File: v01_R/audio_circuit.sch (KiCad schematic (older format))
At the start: 44 parts, among them P1 CONN_1, P10 CONN_1, P11 CONN_1, P12 CONN_1, P2 CONN_1, P3 CONN_1, P4 CONN_1, P5 CONN_1, P6 CONN_1, P7 CONN_1, P8 CONN_1, P9 CONN_1, U2 TI_TPA6138A2

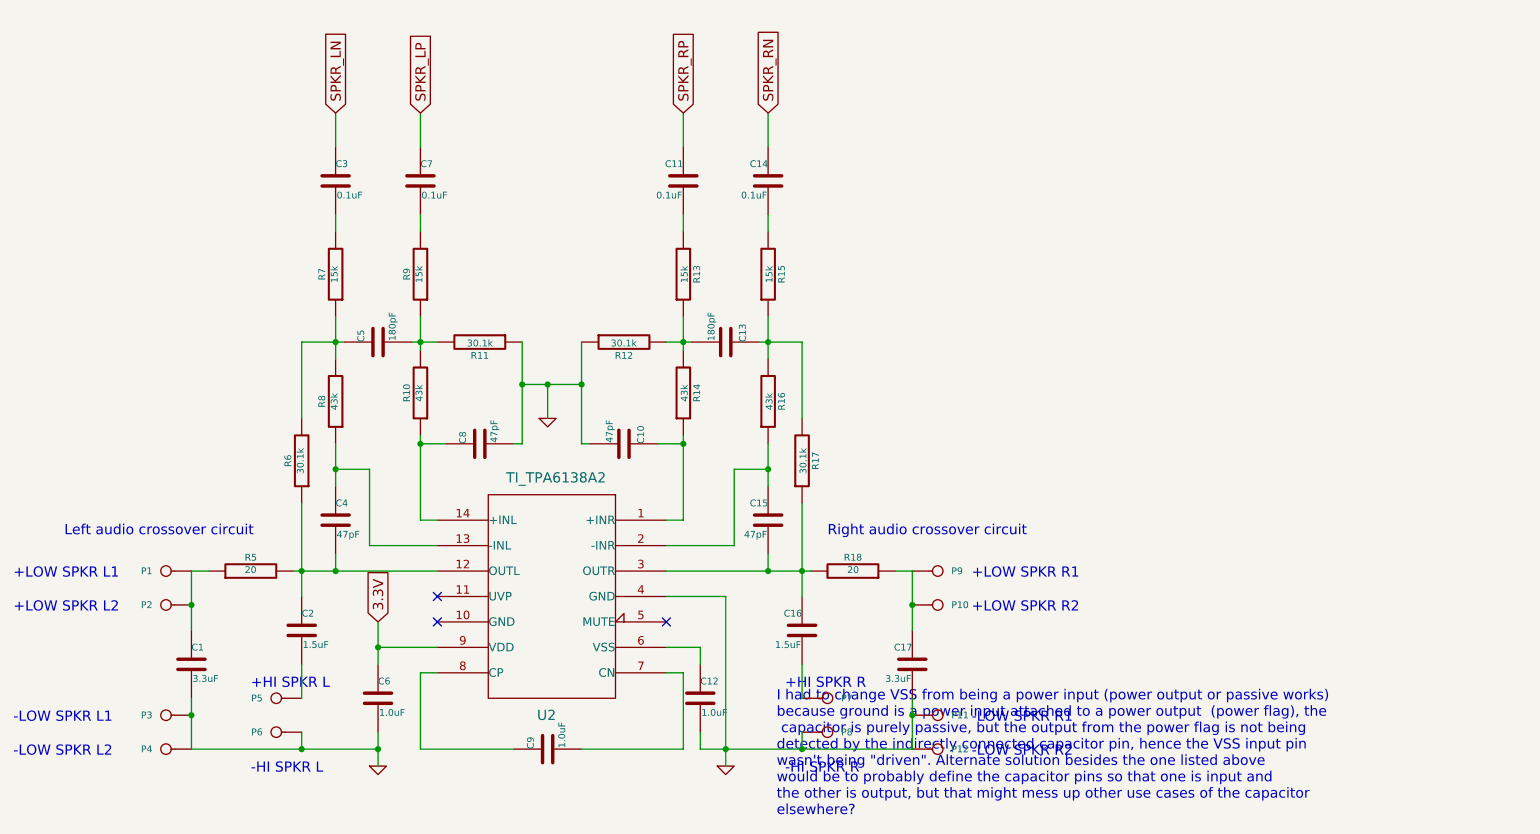
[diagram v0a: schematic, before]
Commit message: Update removes the left channel of the audio circuit.
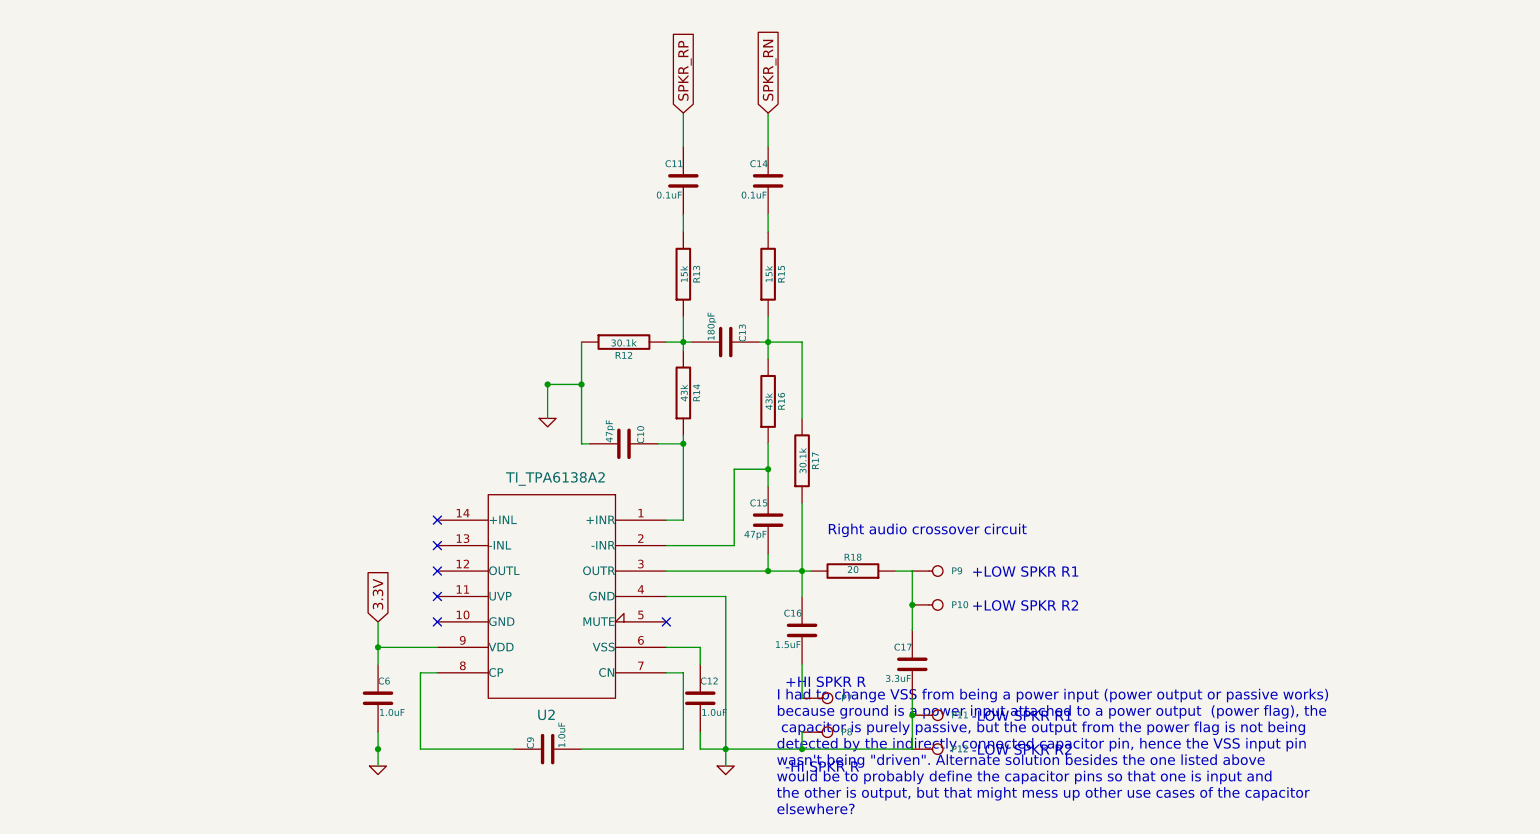
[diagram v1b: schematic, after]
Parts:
- removed C1: 3.3uF, ~, symbol C
- removed C2: 1.5uF, ~, symbol C
- removed C3, C7: 0.1uF, ~, symbol C
- removed C4, C8: 47pF, ~, symbol C
- removed C5: 180pF, ~, symbol C
- removed P1, P2, P3, P4, P5, P6: CONN_1, symbol CONN_1
- removed R10, R8: 43k, ~, symbol R
- removed R11, R6: 30.1k, ~, symbol R
- removed R5: 20, ~, symbol R
- removed R7, R9: 15k, ~, symbol R
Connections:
- no-connect marks 3 -> 6
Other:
- note removed: "+HI SPKR L"
- note removed: "+LOW SPKR L1"
- note removed: "+LOW SPKR L2"
- note removed: "-HI SPKR L"
- note removed: "-LOW SPKR L1"
- note removed: "-LOW SPKR L2"
- note removed: "Left audio crossover circuit"

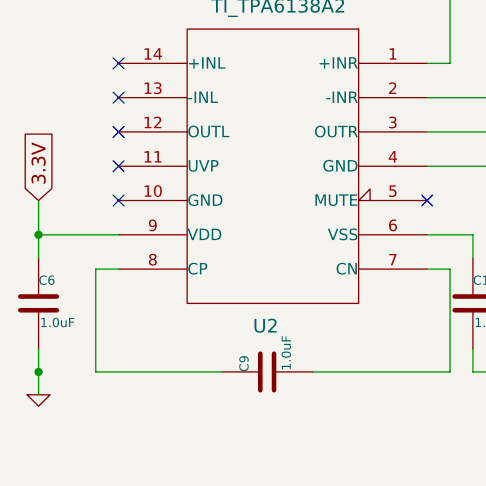
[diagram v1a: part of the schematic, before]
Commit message: Updating entire schematic and footprint selections. Adding jst-ph footprints.
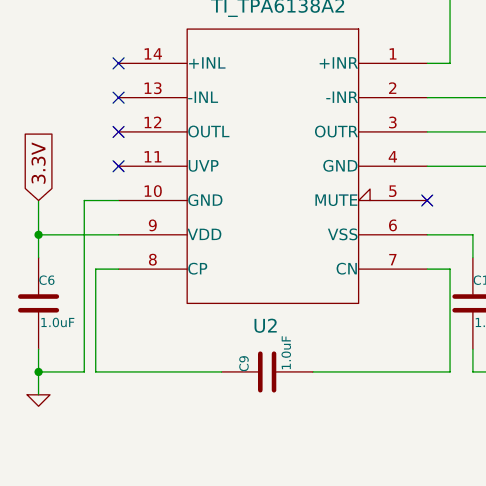
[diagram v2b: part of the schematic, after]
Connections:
- net GND: now also U2.10 (GND)
- no-connect marks 6 -> 5
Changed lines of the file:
@@
 Sheet 2 4
 Title ""
-Date "16 jan 2015"
+Date "17 jan 2015"
 Rev ""
 Comp ""
@@
 $EndComp
 $Comp
-L GND #PWR05
+L GND #PWR04
 U 1 1 541DFF4B
 P 4800 6150
-F 0 "#PWR05" H 4800 6150 30  0001 C CNN
+F 0 "#PWR04" H 4800 6150 30  0001 C CNN
 F 1 "GND" H 4800 6080 30  0001 C CNN
 F 2 "" H 4800 6150 60  0000 C CNN
@@
 $EndComp
 NoConn ~ 5150 5150
-NoConn ~ 5150 5300
-$Comp
-L GND #PWR06
+$Comp
+L GND #PWR05
 U 1 1 541E060D
 P 5800 4100
-F 0 "#PWR06" H 5800 4100 30  0001 C CNN
+F 0 "#PWR05" H 5800 4100 30  0001 C CNN
 F 1 "GND" H 5800 4030 30  0001 C CNN
 F 2 "" H 5800 4100 60  0000 C CNN
@@
 $EndComp
 $Comp
-L GND #PWR07
+L GND #PWR06
 U 1 1 541E08B0
 P 6850 6150
-F 0 "#PWR07" H 6850 6150 30  0001 C CNN
+F 0 "#PWR06" H 6850 6150 30  0001 C CNN
 F 1 "GND" H 6850 6080 30  0001 C CNN
 F 2 "" H 6850 6150 60  0000 C CNN
@@
 	1    0    0    -1
 $EndComp
-NoConn ~ 6500 5300
 Text Notes 7450 4800 0    60   ~ 0
 Right audio crossover circuit
@@
 NoConn ~ 5150 4850
 NoConn ~ 5150 5000
+Wire Wire Line
+	5150 5300 5000 5300
+Wire Wire Line
+	5000 5300 5000 6050
+Wire Wire Line
+	5000 6050 4800 6050
+NoConn ~ 6500 5300
 $EndSCHEMATC

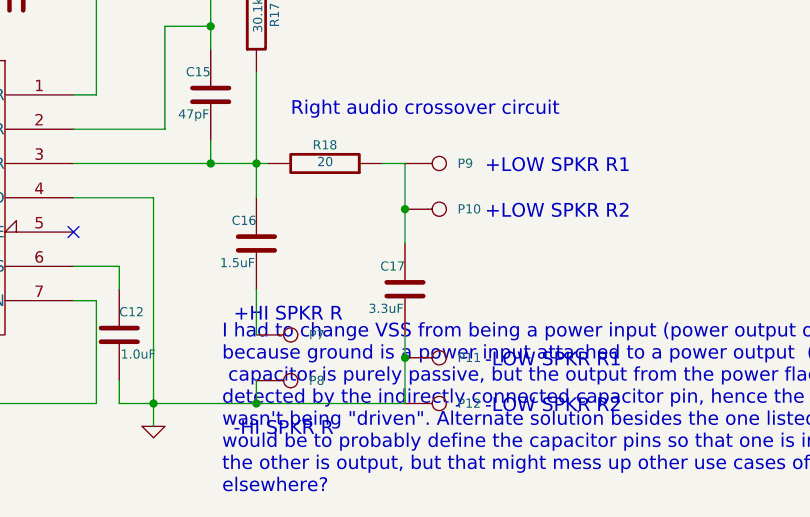
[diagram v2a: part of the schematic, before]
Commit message: Adding very rough initial version of PCB. The BA driver pads were not exact yet (based off of a Sonion driver datasheet).
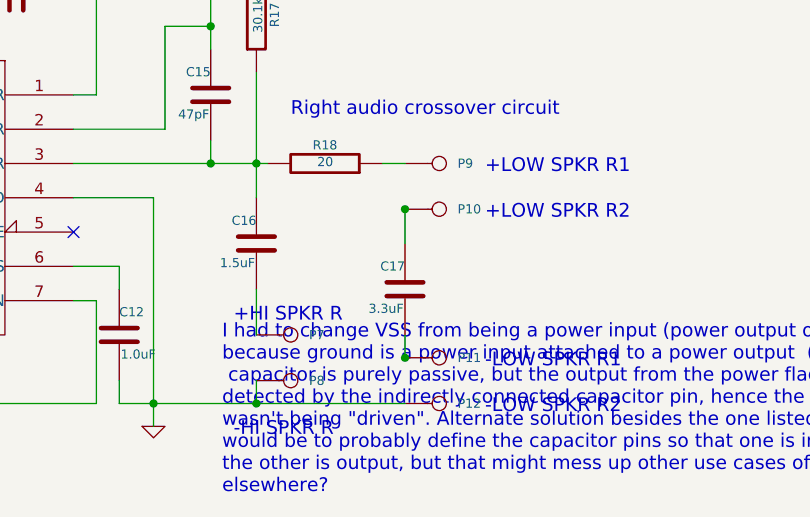
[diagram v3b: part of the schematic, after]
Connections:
- net GND: no longer C17.2, P11.1
- net at C17.1, P10.1: no longer P9.1, R18.1
- new net: C17.2, P11.1
- new net: P9.1, R18.1
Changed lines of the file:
@@
 Sheet 2 4
 Title ""
-Date "17 jan 2015"
+Date "18 jan 2015"
 Rev ""
 Comp ""
@@
 	7300 6050 7300 5950
 Connection ~ 7300 6050
-Wire Wire Line
-	7950 5750 7950 6050
 Connection ~ 7950 5850
-Wire Wire Line
-	7950 5000 7950 5350
 Connection ~ 7950 5200
 Wire Wire Line
@@
 	5000 6050 4800 6050
 NoConn ~ 6500 5300
+Wire Wire Line
+	7950 5200 7950 5350
+Wire Wire Line
+	7950 5750 7950 5850
 $EndSCHEMATC

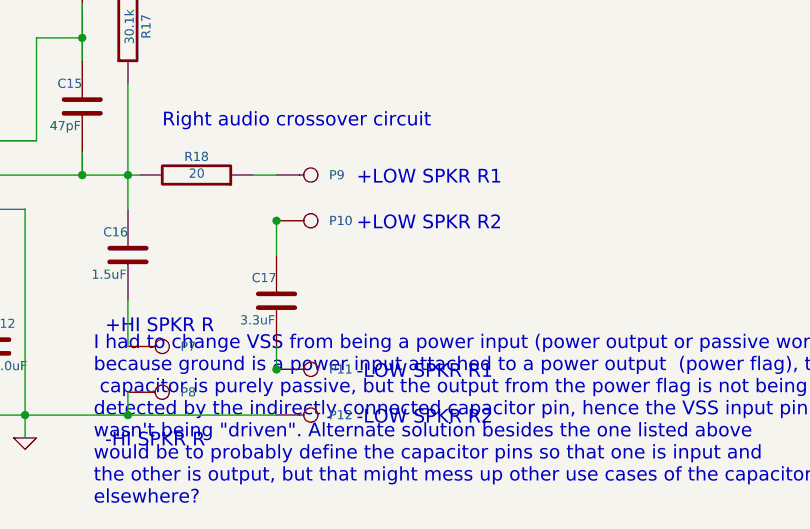
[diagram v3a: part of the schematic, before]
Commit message: Update with 2.00" diameter version of the CWIEM R v01 PCB. The only change remaining was to finalize sound driver pad placement and sizing. After that, production files could be generated for board manufacturing.
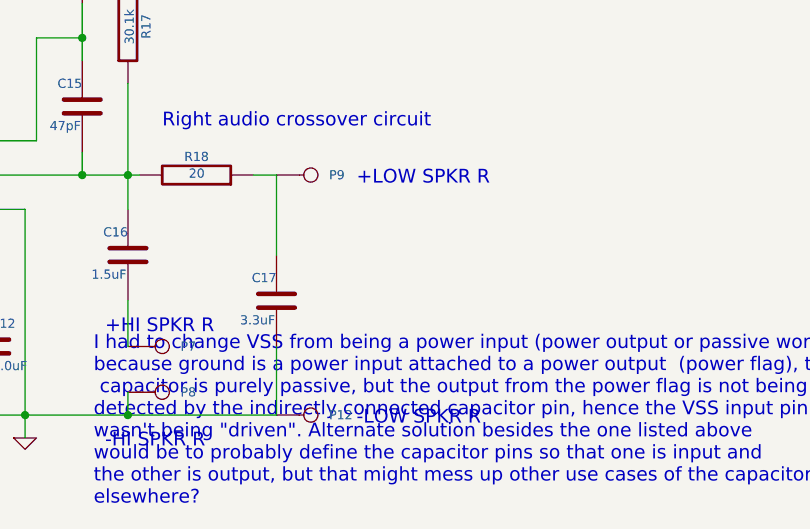
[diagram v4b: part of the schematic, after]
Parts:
- removed P10, P11: CONN_1, symbol CONN_1
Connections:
- net GND: now also C17.2
- net at C17.1: now also P9.1, R18.1
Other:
- note added: "+LOW SPKR R"
- note added: "-LOW SPKR R"
- note removed: "+LOW SPKR R1"
- note removed: "+LOW SPKR R2"
- note removed: "-LOW SPKR R1"
- note removed: "-LOW SPKR R2"
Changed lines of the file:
@@
 LIBS:ab2_usb
 LIBS:jst-ph
+LIBS:shardy
+LIBS:tps63031
+LIBS:tps73601dbvr
 LIBS:CWIEM_PCB_v01_R-cache
 EELAYER 27 0
@@
 Sheet 2 4
 Title ""
-Date "18 jan 2015"
+Date "25 jan 2015"
 Rev ""
 Comp ""
@@
 $EndComp
 $Comp
-L CONN_1 P11
-U 1 1 541E07A8
-P 8100 5850
-F 0 "P11" H 8180 5850 40  0000 L CNN
-F 1 "CONN_1" H 8100 5905 30  0001 C CNN
-F 2 "" H 8100 5850 60  0000 C CNN
-F 3 "" H 8100 5850 60  0000 C CNN
-	1    8100 5850
-	1    0    0    1
-$EndComp
-$Comp
 L C C17
 U 1 1 541E07AF
@@
 	1    7950 5550
 	-1   0    0    -1
-$EndComp
-$Comp
-L CONN_1 P10
-U 1 1 541E07B6
-P 8100 5200
-F 0 "P10" H 8180 5200 40  0000 L CNN
-F 1 "CONN_1" H 8100 5255 30  0001 C CNN
-F 2 "" H 8100 5200 60  0000 C CNN
-F 3 "" H 8100 5200 60  0000 C CNN
-	1    8100 5200
-	1    0    0    1
 $EndComp
 $Comp
@@
 Right audio crossover circuit
 Text Notes 8300 5050 0    60   ~ 0
-+LOW SPKR R1
-Text Notes 8300 5250 0    60   ~ 0
-+LOW SPKR R2
-Text Notes 8300 5900 0    60   ~ 0
--LOW SPKR R1
++LOW SPKR R
 Text Notes 8300 6100 0    60   ~ 0
--LOW SPKR R2
+-LOW SPKR R
 Text GLabel 6600 2300 1    60   Input ~ 0
 SPKR_RP
@@
 	7300 6050 7300 5950
 Connection ~ 7300 6050
-Connection ~ 7950 5850
-Connection ~ 7950 5200
 Wire Wire Line
 	7850 5000 7950 5000
@@
 NoConn ~ 6500 5300
 Wire Wire Line
-	7950 5200 7950 5350
-Wire Wire Line
-	7950 5750 7950 5850
+	7950 5000 7950 5350
+Wire Wire Line
+	7950 5750 7950 6050
 $EndSCHEMATC
